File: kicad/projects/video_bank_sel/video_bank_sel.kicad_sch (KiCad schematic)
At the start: 26 parts, among them J1 peripheral_addr_bus_connector, J2 peripheral_aux_connector, J3 peripheral_membank_connector, J4 Conn_01x16_Socket, J5 Conn_01x16_Socket, J6 Conn_01x16_Socket, U1 74HC245, U10 74HC245, U11 74HC245, U12 74HC08, U13 74HC00, U14 74HC32, U2 74HC245, U3 74HC245, U4 74HC245, U5 74HC245, U6 74HC245, U7 74HC138, U8 74HC377, U9 74HC377

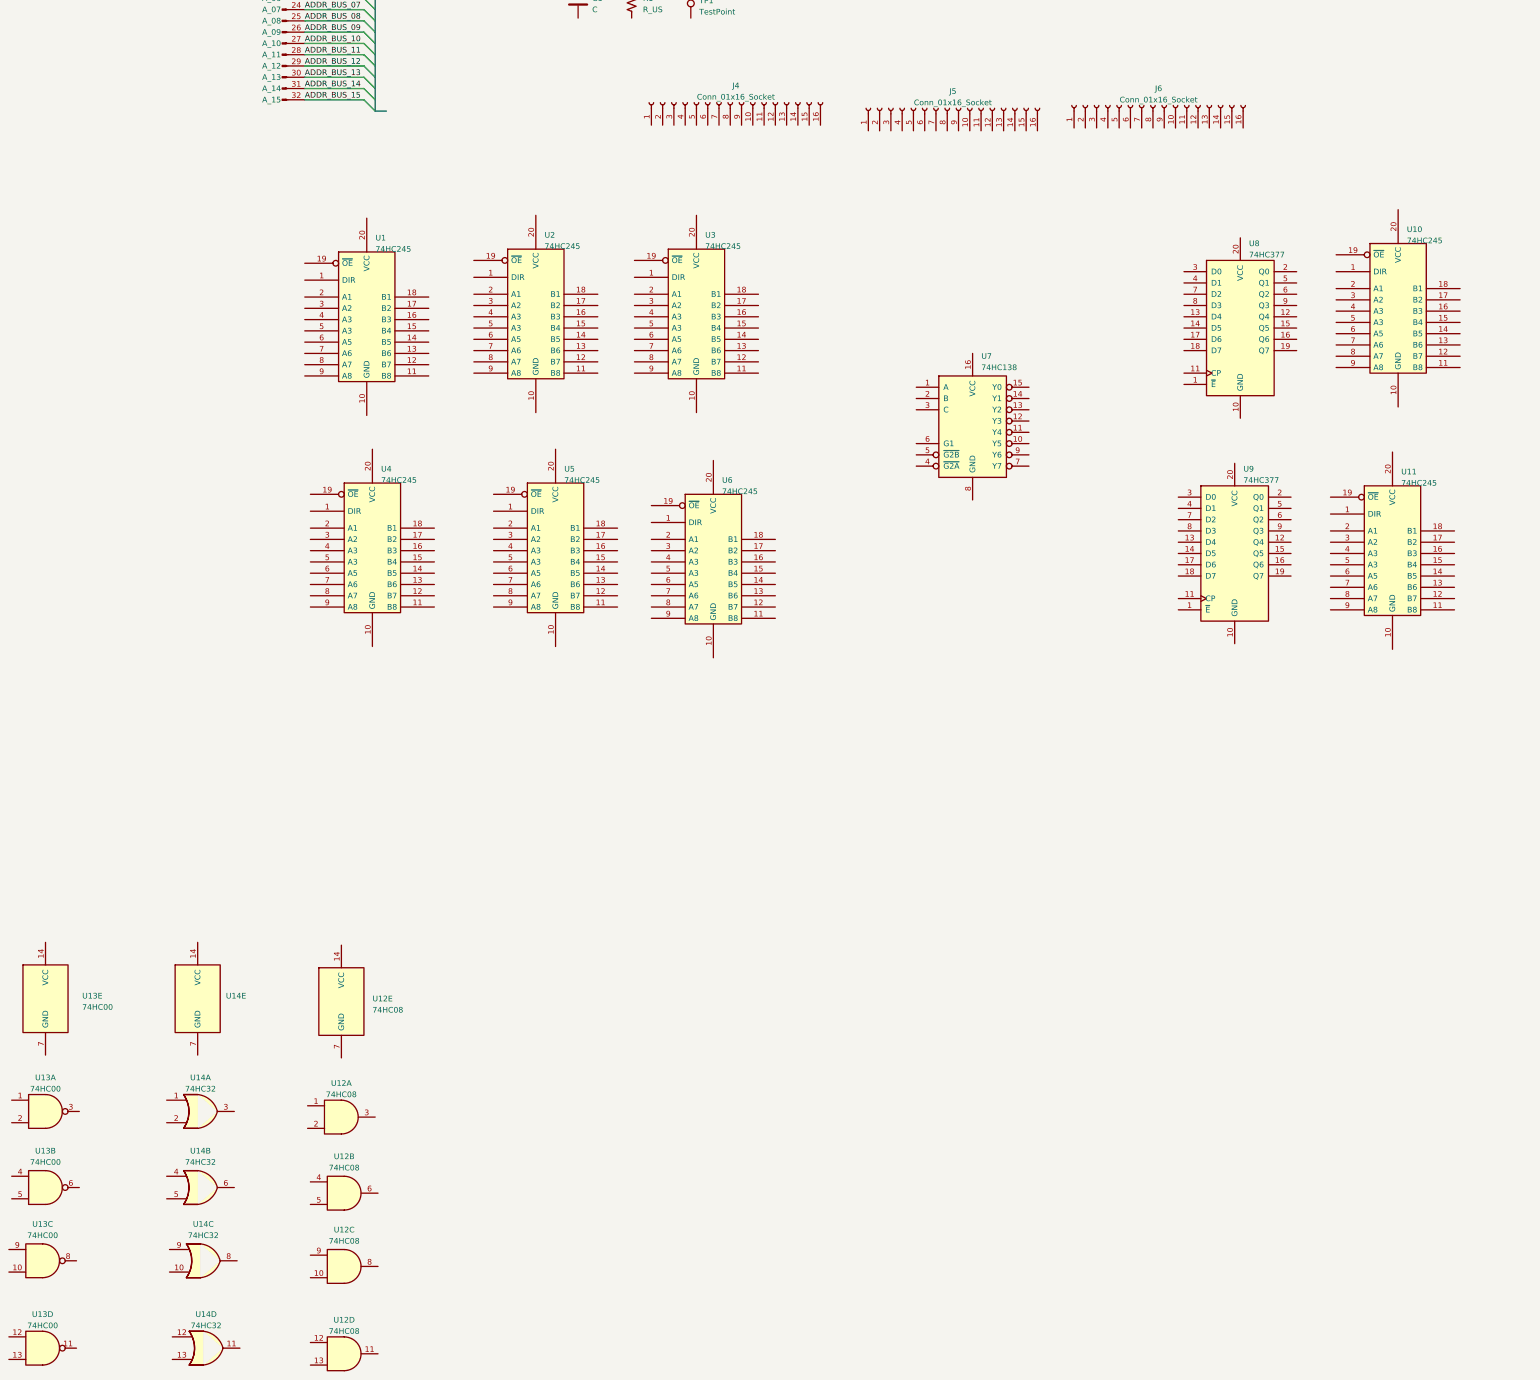
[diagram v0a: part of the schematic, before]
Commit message: Roughing out the video baords - time to switch to 157s for bank sel as well.
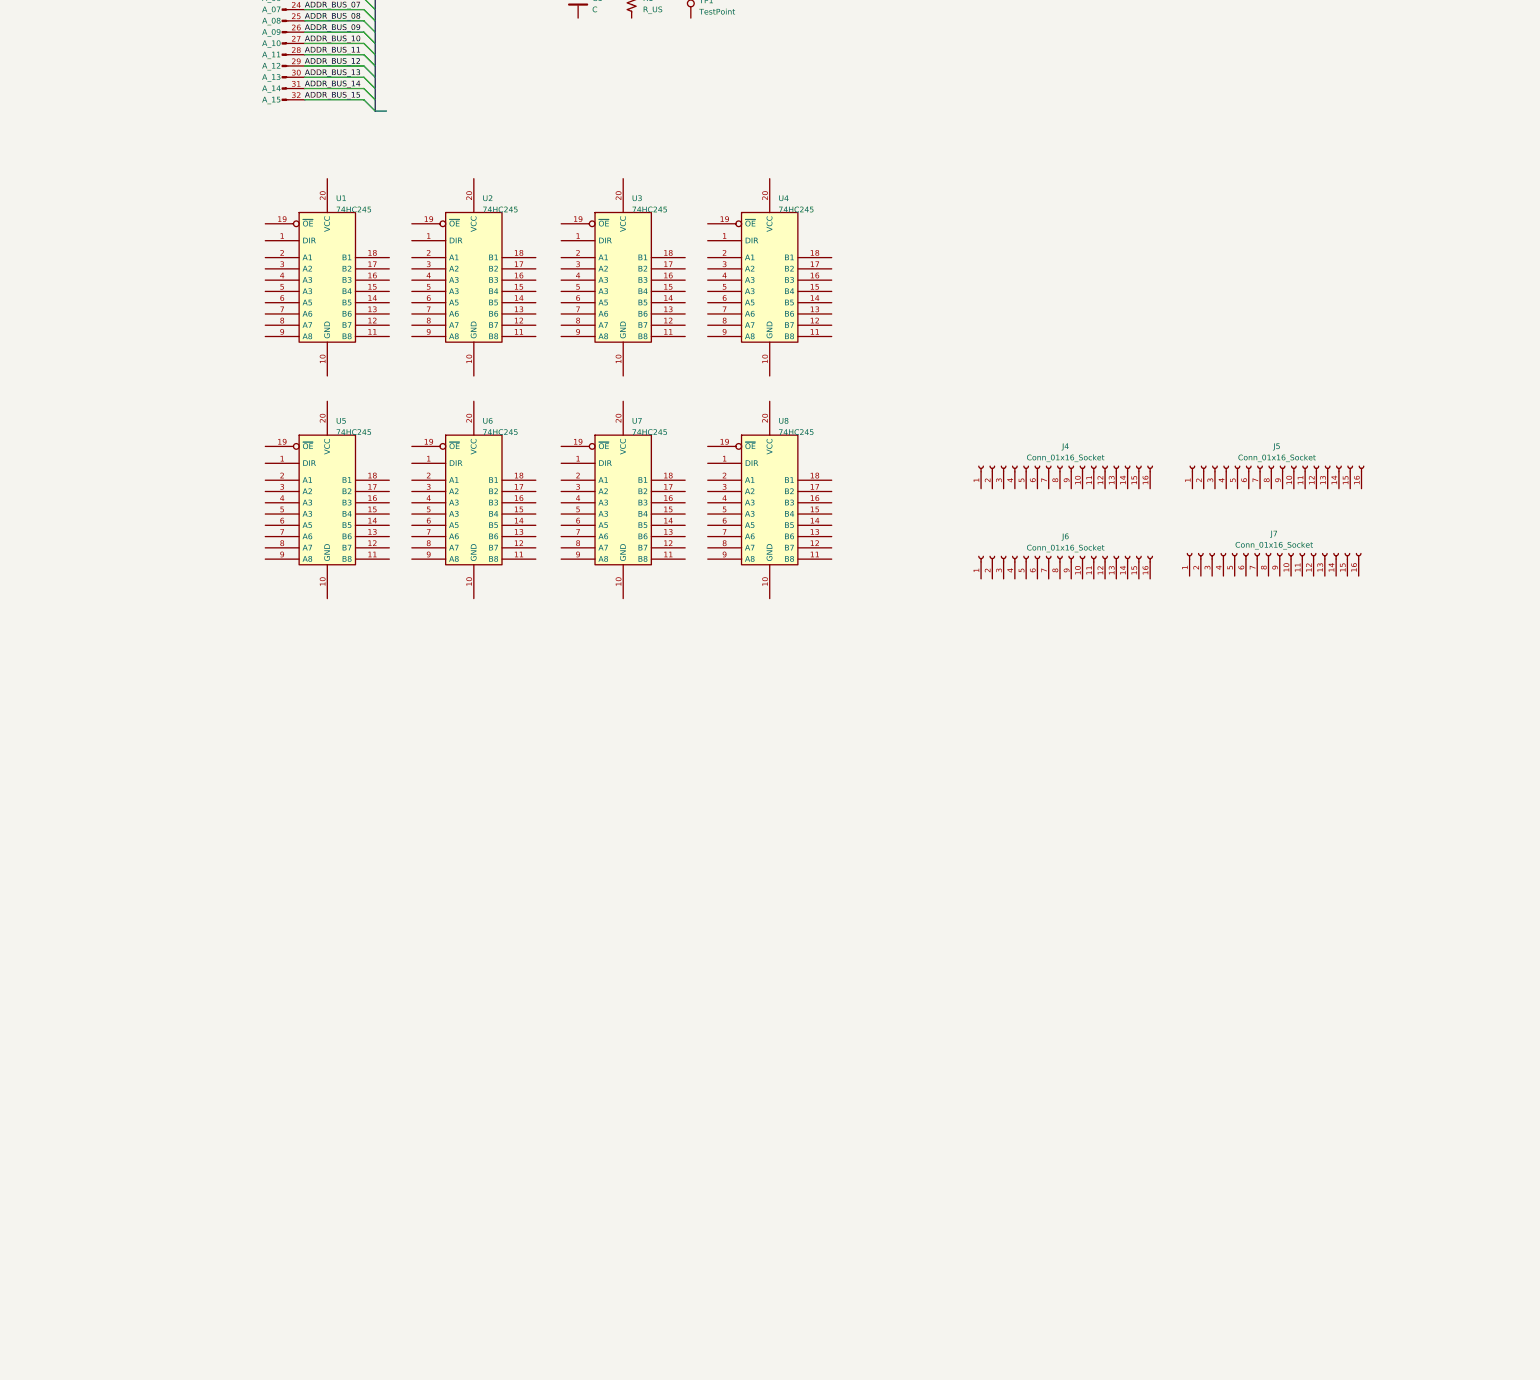
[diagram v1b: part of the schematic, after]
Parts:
- removed U10, U11: 74HC245, Package_DIP:DIP-20_W7.62mm_Socket, symbol sixteen-bit-computer:74HC245
- removed U12: 74HC08, Package_DIP:DIP-14_W7.62mm_Socket, symbol sixteen-bit-computer:74HC08
- removed U13: 74HC00, Package_DIP:DIP-14_W7.62mm_Socket, symbol 74xx:74HC00
- removed U14: 74HC32, Package_DIP:DIP-14_W7.62mm_Socket, symbol sixteen-bit-computer:74HC32
- removed U7: 74HC138, Package_DIP:DIP-16_W7.62mm_Socket, symbol sixteen-bit-computer:74HC138
- removed U8, U9: 74HC377, Package_DIP:DIP-20_W7.62mm_Socket, symbol sixteen-bit-computer:74HC377
- added J7: Conn_01x16_Socket, Connector_PinSocket_2.54mm:PinSocket_1x16_P2.54mm_Horizontal, symbol Connector:Conn_01x16_Socket
- added U7, U8: 74HC245, Package_DIP:DIP-20_W7.62mm_Socket, symbol sixteen-bit-computer:74HC245
